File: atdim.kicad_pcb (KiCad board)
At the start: 2 copper layers, 49.8 x 24.9 mm, 19 parts, among them IC1 ATTINY85-T, P1 CONN_4, P2 ICSP, Q1 MOSFET_N, U1 7805

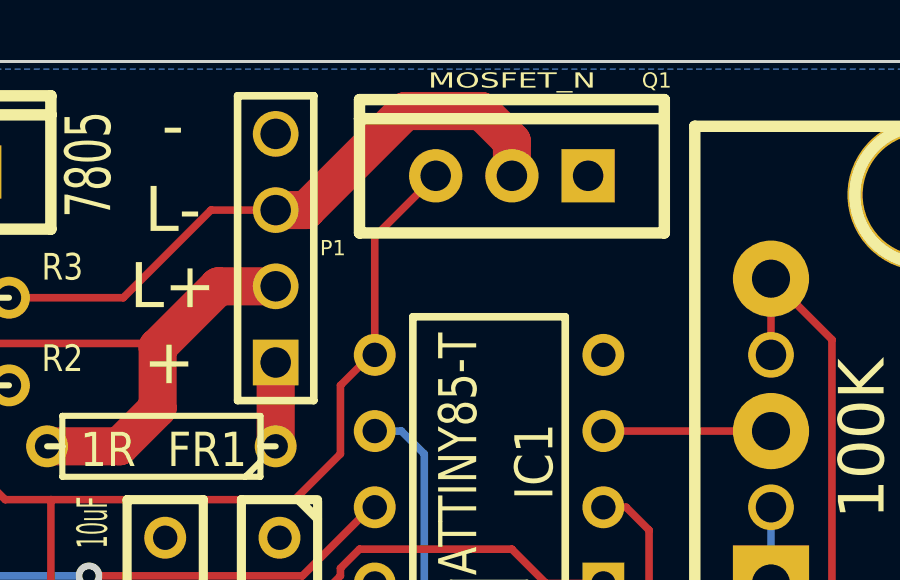
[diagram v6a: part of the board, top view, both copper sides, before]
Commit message: add a freewheel diode just in case I ever want to use this for motor control
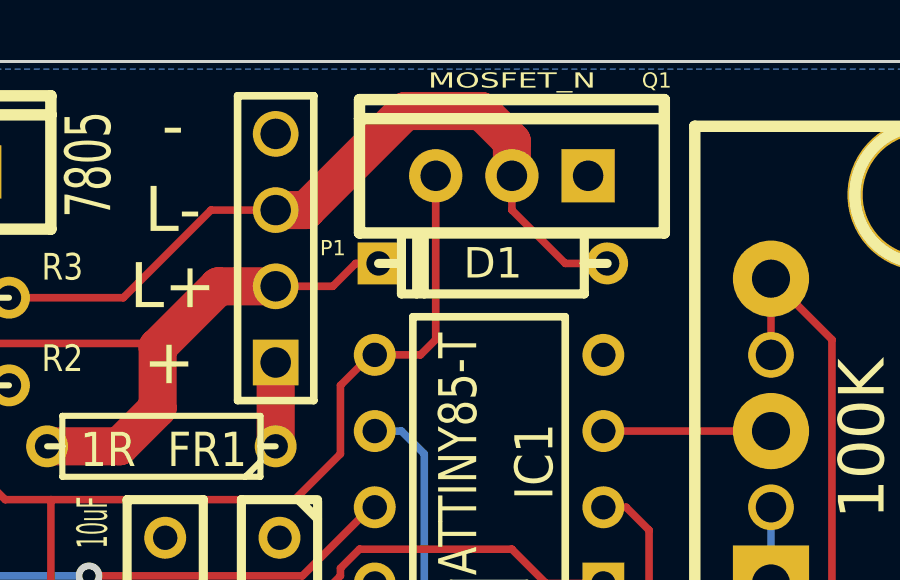
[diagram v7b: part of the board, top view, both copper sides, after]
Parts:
- added D1: DIODE, D3, F.Cu at (132.0, 106.8)
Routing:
- net /DRAIN: track 20.9 -> 26.0 mm
- net /+12VS: track 41.6 -> 45.3 mm
- net /MOSI: track 34.1 -> 35.0 mm
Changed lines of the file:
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@@
 (kicad_pcb (version 3) (host pcbnew "(2013-june-11)-stable")
   (general
-    (links 36)
+    (links 38)
     (no_connects 0)
     (area 99.2505 99.8855 150.241 125.1966)
     (thickness 1.6)
     (drawings 9)
-    (tracks 108)
+    (tracks 115)
     (zones 0)
-    (modules 19)
+    (modules 20)
     (nets 12)
   )
@@
     )
   )
+  (module D3 (layer F.Cu)
+    (at 131.953 106.807 180)
+    (descr "Diode 3 pas")
+    (tags "DIODE DEV")
+    (fp_text reference D1 (at 0 0 180) (layer F.SilkS)
+      (effects (font (size 1.016 1.016) (thickness 0.2032)))
+    )
+    (fp_text value DIODE (at 0 0 180) (layer F.SilkS) hide
+      (effects (font (size 1.016 1.016) (thickness 0.2032)))
+    )
+    (fp_line (start 3.81 0) (end 3.048 0) (layer F.SilkS) (width 0.3048))
+    (fp_line (start 3.048 0) (end 3.048 -1.016) (layer F.SilkS) (width 0.3048))
+    (fp_line (start 3.048 -1.016) (end -3.048 -1.016) (layer F.SilkS) (width 0.3048))
+    (fp_line (start -3.048 -1.016) (end -3.048 0) (layer F.SilkS) (width 0.3048))
+    (fp_line (start -3.048 0) (end -3.81 0) (layer F.SilkS) (width 0.3048))
+    (fp_line (start -3.048 0) (end -3.048 1.016) (layer F.SilkS) (width 0.3048))
+    (fp_line (start -3.048 1.016) (end 3.048 1.016) (layer F.SilkS) (width 0.3048))
+    (fp_line (start 3.048 1.016) (end 3.048 0) (layer F.SilkS) (width 0.3048))
+    (fp_line (start 2.54 -1.016) (end 2.54 1.016) (layer F.SilkS) (width 0.3048))
+    (fp_line (start 2.286 1.016) (end 2.286 -1.016) (layer F.SilkS) (width 0.3048))
+    (pad 2 thru_hole rect (at 3.81 0 180) (size 1.397 1.397) (drill 0.8128)
+      (layers *.Cu *.Mask F.SilkS)
+      (net 2 /+12VS)
+    )
+    (pad 1 thru_hole circle (at -3.81 0 180) (size 1.397 1.397) (drill 0.8128)
+      (layers *.Cu *.Mask F.SilkS)
+      (net 5 /DRAIN)
+    )
+    (model discret/diode.wrl
+      (at (xyz 0 0 0))
+      (scale (xyz 0.3 0.3 0.3))
+      (rotate (xyz 0 0 0))
+    )
+  )
   (gr_text "GND   SCK   VCC MISO  MOSI  ~RESET" (at 113.665 124.079) (layer F.SilkS)
     (effects (font (size 0.5 0.5) (thickness 0.125)))
@@
   (gr_line (start 100.076 100.076) (end 149.86 100.076) (angle 90) (layer Edge.Cuts) (width 0.1))
   (segment (start 124.714 110.109) (end 124.714 112.903) (width 1.27) (layer F.Cu) (net 1))
+  (segment (start 128.143 106.807) (end 127.381 106.807) (width 0.254) (layer F.Cu) (net 2) (status 400000))
+  (segment (start 126.619 107.569) (end 124.714 107.569) (width 0.254) (layer F.Cu) (net 2) (status 800000))
+  (segment (start 127.381 106.807) (end 126.619 107.569) (width 0.254) (layer F.Cu) (net 2))
   (segment (start 105.283 109.855) (end 105.283 108.077) (width 0.254) (layer F.Cu) (net 2))
   (segment (start 105.283 108.077) (end 109.601 103.759) (width 0.254) (layer F.Cu) (net 2))
@@
   (segment (start 137.16 115.697) (end 137.16 121.793) (width 0.254) (layer F.Cu) (net 4))
   (segment (start 136.398 114.935) (end 137.16 115.697) (width 0.254) (layer F.Cu) (net 4))
+  (segment (start 135.763 106.807) (end 134.366 106.807) (width 0.254) (layer F.Cu) (net 5) (status 400000))
+  (segment (start 132.588 105.029) (end 132.588 103.886) (width 0.254) (layer F.Cu) (net 5) (status 800000))
+  (segment (start 134.366 106.807) (end 132.588 105.029) (width 0.254) (layer F.Cu) (net 5))
   (segment (start 115.824 107.95) (end 119.634 107.95) (width 0.254) (layer F.Cu) (net 5))
   (segment (start 122.555 105.029) (end 124.714 105.029) (width 0.254) (layer F.Cu) (net 5))
@@
   (segment (start 129.667 113.157) (end 129.667 120.396) (width 0.254) (layer B.Cu) (net 6))
   (segment (start 128.905 112.395) (end 129.667 113.157) (width 0.254) (layer B.Cu) (net 6))
-  (segment (start 115.824 110.871) (end 115.062 111.633) (width 0.254) (layer F.Cu) (net 7) (status 400000))
+  (segment (start 130.048 103.886) (end 130.048 109.347) (width 0.254) (layer F.Cu) (net 7))
+  (segment (start 129.54 109.855) (end 128.016 109.855) (width 0.254) (layer F.Cu) (net 7))
+  (segment (start 130.048 109.347) (end 129.54 109.855) (width 0.254) (layer F.Cu) (net 7))
+  (segment (start 115.824 110.871) (end 115.062 111.633) (width 0.254) (layer F.Cu) (net 7))
   (segment (start 115.697 114.681) (end 117.221 114.681) (width 0.254) (layer F.Cu) (net 7))
   (segment (start 115.062 114.046) (end 115.697 114.681) (width 0.254) (layer F.Cu) (net 7))
@@
   (segment (start 117.221 121.92) (end 117.221 114.681) (width 0.254) (layer F.Cu) (net 7))
   (segment (start 117.221 114.681) (end 117.221 114.681) (width 0.254) (layer F.Cu) (net 7))
-  (segment (start 130.048 103.886) (end 128.016 105.918) (width 0.254) (layer F.Cu) (net 7))
-  (segment (start 128.016 105.918) (end 128.016 109.855) (width 0.254) (layer F.Cu) (net 7))
   (segment (start 128.016 114.935) (end 127.889 114.935) (width 0.254) (layer F.Cu) (net 8))
   (segment (start 109.601 121.539) (end 109.601 121.92) (width 0.254) (layer F.Cu) (net 8))

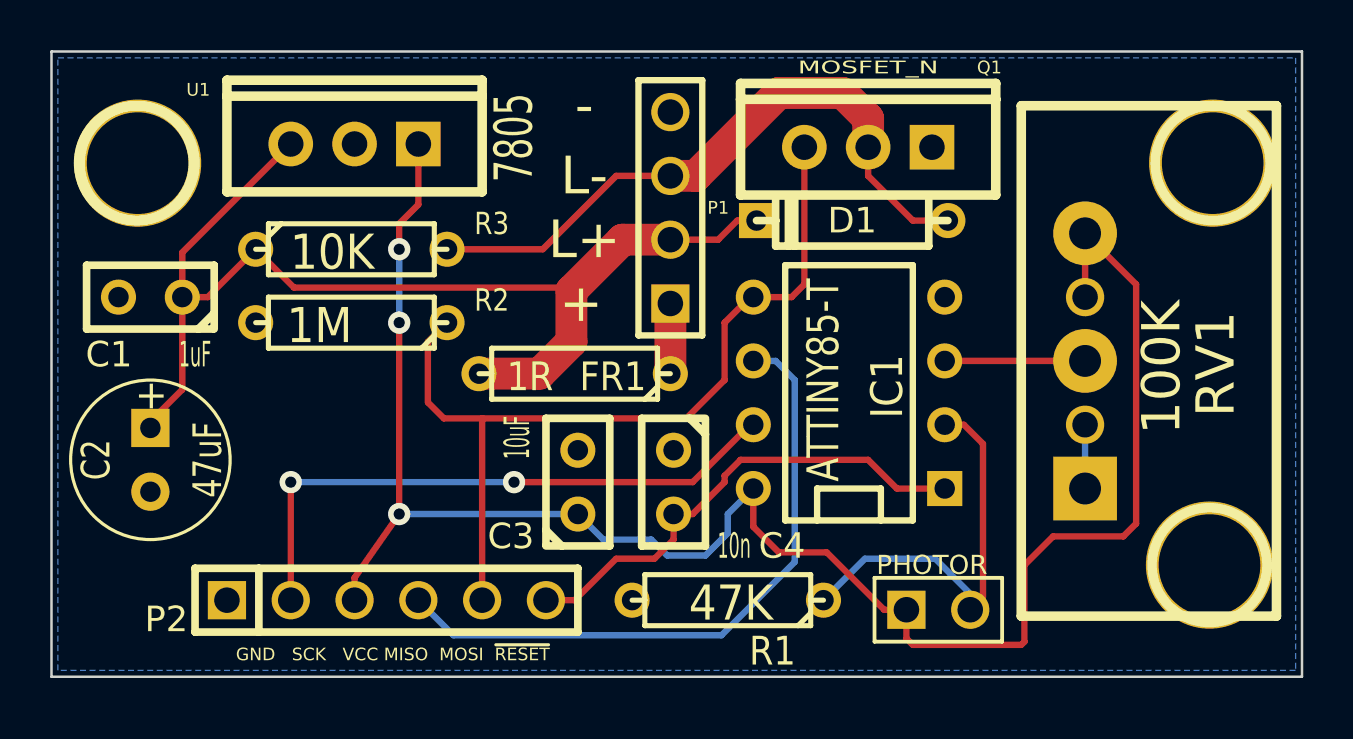
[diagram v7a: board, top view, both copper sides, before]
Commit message: increase trace width for higher power
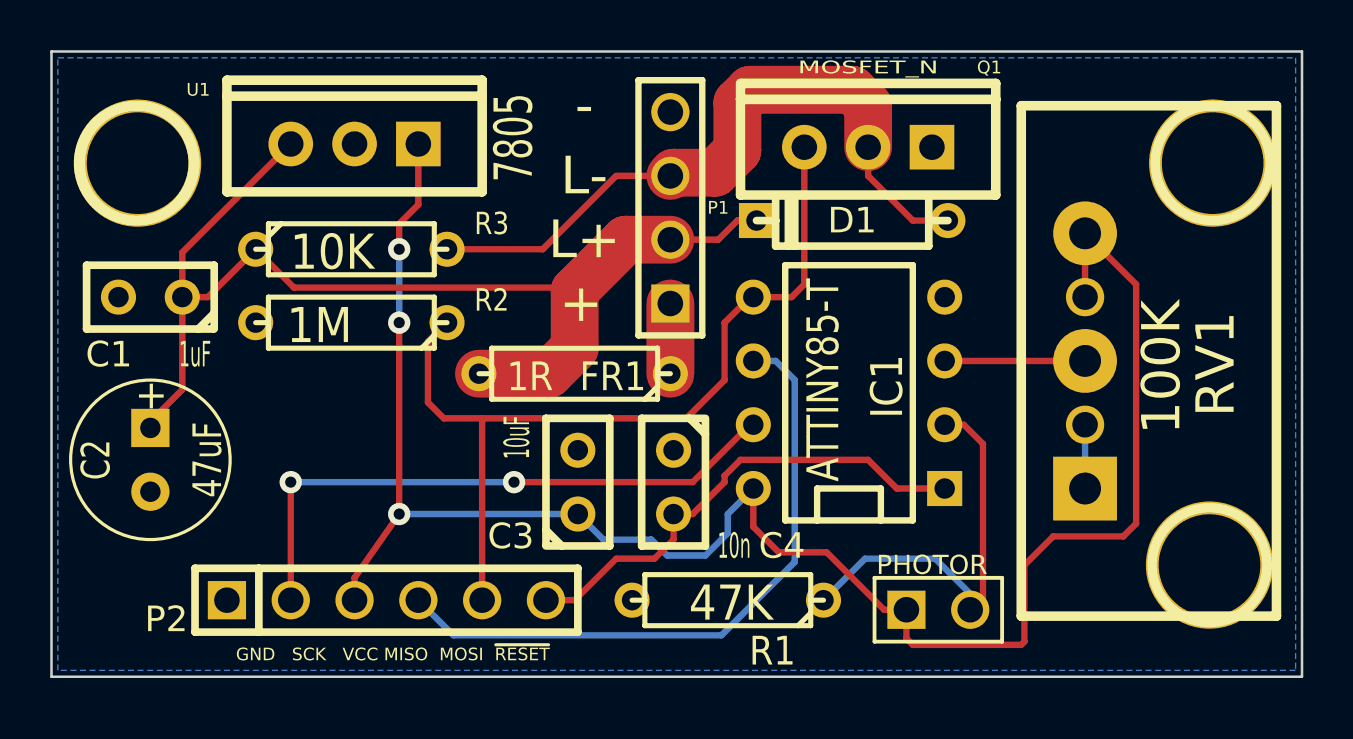
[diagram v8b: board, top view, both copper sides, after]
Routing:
- net /DRAIN: track 26.0 -> 27.5 mm
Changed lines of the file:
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@@
     (thickness 1.6)
     (drawings 9)
-    (tracks 115)
+    (tracks 118)
     (zones 0)
     (modules 20)
@@
   )
   (setup
-    (last_trace_width 0.254)
+    (last_trace_width 1.905)
     (user_trace_width 0.254)
     (user_trace_width 1.27)
+    (user_trace_width 1.905)
     (trace_clearance 0.254)
     (zone_clearance 0.508)
@@
   (gr_line (start 149.86 100.076) (end 149.86 124.968) (angle 90) (layer Edge.Cuts) (width 0.1))
   (gr_line (start 100.076 100.076) (end 149.86 100.076) (angle 90) (layer Edge.Cuts) (width 0.1))
-  (segment (start 124.714 110.109) (end 124.714 112.903) (width 1.27) (layer F.Cu) (net 1))
-  (segment (start 128.143 106.807) (end 127.381 106.807) (width 0.254) (layer F.Cu) (net 2) (status 400000))
-  (segment (start 126.619 107.569) (end 124.714 107.569) (width 0.254) (layer F.Cu) (net 2) (status 800000))
+  (segment (start 124.714 112.903) (end 124.714 110.109) (width 1.905) (layer F.Cu) (net 1))
+  (segment (start 108.204 107.95) (end 109.728 109.474) (width 0.254) (layer F.Cu) (net 2))
+  (segment (start 120.777 109.474) (end 120.904 109.601) (width 0.254) (layer F.Cu) (net 2))
+  (segment (start 109.728 109.474) (end 120.777 109.474) (width 0.254) (layer F.Cu) (net 2))
+  (segment (start 124.714 107.569) (end 122.936 107.569) (width 1.905) (layer F.Cu) (net 2))
+  (segment (start 122.936 107.569) (end 120.904 109.601) (width 1.905) (layer F.Cu) (net 2))
+  (segment (start 119.888 112.903) (end 117.094 112.903) (width 1.905) (layer F.Cu) (net 2))
+  (segment (start 120.904 109.601) (end 120.904 111.887) (width 1.905) (layer F.Cu) (net 2))
+  (segment (start 120.904 111.887) (end 119.888 112.903) (width 1.905) (layer F.Cu) (net 2))
+  (segment (start 128.143 106.807) (end 127.381 106.807) (width 0.254) (layer F.Cu) (net 2))
+  (segment (start 126.619 107.569) (end 124.714 107.569) (width 0.254) (layer F.Cu) (net 2))
   (segment (start 127.381 106.807) (end 126.619 107.569) (width 0.254) (layer F.Cu) (net 2))
   (segment (start 105.283 109.855) (end 105.283 108.077) (width 0.254) (layer F.Cu) (net 2))
   (segment (start 105.283 108.077) (end 109.601 103.759) (width 0.254) (layer F.Cu) (net 2))
-  (segment (start 108.204 107.95) (end 109.728 109.474) (width 0.254) (layer F.Cu) (net 2))
-  (segment (start 120.65 109.474) (end 120.777 109.601) (width 0.254) (layer F.Cu) (net 2))
-  (segment (start 109.728 109.474) (end 120.65 109.474) (width 0.254) (layer F.Cu) (net 2))
-  (segment (start 117.094 112.903) (end 119.507 112.903) (width 1.27) (layer F.Cu) (net 2))
-  (segment (start 119.507 112.903) (end 120.777 111.633) (width 1.27) (layer F.Cu) (net 2))
-  (segment (start 120.777 111.633) (end 120.777 109.601) (width 1.27) (layer F.Cu) (net 2))
-  (segment (start 122.809 107.569) (end 124.714 107.569) (width 1.27) (layer F.Cu) (net 2))
-  (segment (start 120.777 109.601) (end 122.809 107.569) (width 1.27) (layer F.Cu) (net 2))
   (segment (start 105.283 109.855) (end 106.299 109.855) (width 0.254) (layer F.Cu) (net 2))
   (segment (start 106.299 109.855) (end 108.204 107.95) (width 0.254) (layer F.Cu) (net 2))
@@
   (segment (start 137.16 115.697) (end 137.16 121.793) (width 0.254) (layer F.Cu) (net 4))
   (segment (start 136.398 114.935) (end 137.16 115.697) (width 0.254) (layer F.Cu) (net 4))
-  (segment (start 135.763 106.807) (end 134.366 106.807) (width 0.254) (layer F.Cu) (net 5) (status 400000))
-  (segment (start 132.588 105.029) (end 132.588 103.886) (width 0.254) (layer F.Cu) (net 5) (status 800000))
+  (segment (start 132.588 103.886) (end 132.588 102.235) (width 1.905) (layer F.Cu) (net 5) (status 400000))
+  (segment (start 124.841 104.902) (end 124.714 105.029) (width 1.905) (layer F.Cu) (net 5) (status C00000))
+  (segment (start 126.492 104.902) (end 124.841 104.902) (width 1.905) (layer F.Cu) (net 5) (status 800000))
+  (segment (start 127.381 104.013) (end 126.492 104.902) (width 1.905) (layer F.Cu) (net 5))
+  (segment (start 127.381 102.108) (end 127.381 104.013) (width 1.905) (layer F.Cu) (net 5))
+  (segment (start 127.889 101.6) (end 127.381 102.108) (width 1.905) (layer F.Cu) (net 5))
+  (segment (start 131.953 101.6) (end 127.889 101.6) (width 1.905) (layer F.Cu) (net 5))
+  (segment (start 132.588 102.235) (end 131.953 101.6) (width 1.905) (layer F.Cu) (net 5))
+  (segment (start 135.763 106.807) (end 134.366 106.807) (width 0.254) (layer F.Cu) (net 5))
+  (segment (start 132.588 105.029) (end 132.588 103.886) (width 0.254) (layer F.Cu) (net 5))
   (segment (start 134.366 106.807) (end 132.588 105.029) (width 0.254) (layer F.Cu) (net 5))
   (segment (start 115.824 107.95) (end 119.634 107.95) (width 0.254) (layer F.Cu) (net 5))
   (segment (start 122.555 105.029) (end 124.714 105.029) (width 0.254) (layer F.Cu) (net 5))
   (segment (start 119.634 107.95) (end 122.555 105.029) (width 0.254) (layer F.Cu) (net 5))
-  (segment (start 132.588 103.886) (end 132.588 102.743) (width 1.27) (layer F.Cu) (net 5))
-  (segment (start 125.73 105.029) (end 124.714 105.029) (width 1.27) (layer F.Cu) (net 5))
-  (segment (start 129.032 101.727) (end 125.73 105.029) (width 1.27) (layer F.Cu) (net 5))
-  (segment (start 131.572 101.727) (end 129.032 101.727) (width 1.27) (layer F.Cu) (net 5))
-  (segment (start 132.588 102.743) (end 131.572 101.727) (width 1.27) (layer F.Cu) (net 5))
   (segment (start 128.016 112.395) (end 128.905 112.395) (width 0.254) (layer B.Cu) (net 6))
   (segment (start 116.078 123.317) (end 114.681 121.92) (width 0.254) (layer B.Cu) (net 6))
